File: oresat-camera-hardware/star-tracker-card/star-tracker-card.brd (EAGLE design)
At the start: 99.8 x 94.7 mm, 319 parts, among them J1 ORESAT-DEBUG-CONNECTOR-CARD, J100 DM3BT-DSF-PEJS, J101 3-1734592-64-1734592-0, J102 FTSH-105-XX-X-DV-K, J4 TFM-120-01-L-D-RA, Q1 MMBT2907, Q2 PMV45EN, Q3 DMP2240UDM, Q4 PMV45EN, Q5 MOSFET-PCH-SOT23-6, Q6 MOSFET-PCH-SOT23-6, U1 RCLAMP0504FB, U10 TLVH431, U11 TCAN330, U12 MIC842LYC5, U13 MIC842LYC5, U14 MAX4211FETE, U15 TPS62112, U16 MAX7310ATE, U2 TPS2051CDBVR, U4 SN74LVC1G07DCK, U5 SN74LVC8T245MPWREPPW24-M, U6 CLVCH16T245MDGGREP, U7 OSD3358-512M-BSM, U8 TLV70028QDDCRQ1, U9 TCA9509DGKRDGK8-M, Y1 24MHz, Y2 ABS07-32.768KHZ-T

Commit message: implemented design review changes. Cleaned up the repo a bit. Added generic SPI EEPROM footprint for booting
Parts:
- removed J2: (no value), SparkFun-Connectors:1X02_LONGPADS
- removed TP32, TP33, TP34: TEST-POINT3X4, SparkFun-Connectors:PAD.03X.04
- added C40: 0.1uF, oresat-rcl:.0603-A
- added JP1: JUMPER-SMT_2_NO_SILK, SparkFun-Jumpers:SMT-JUMPER_2_NO_SILK
- added TP67, TP68: TEST-POINT, Tova:2MM-TEST-POINT
- added TP69: TEST-POINT3X4, SparkFun-Connectors:PAD.03X.04
- added U17: 25AAXX, U-Generic-SPI-EEPROM:SOIC8
- R59, R60: value 47k -> DNP
- moved R59 65.2 mm to (81.5, 59.5), turned to 180 degrees
- moved R60 64.1 mm to (81.5, 57.5), turned to 0 degrees
- moved TP31 59.6 mm to (7.50, 57.5)
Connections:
- removed net 5V_IN: C14.1, J2.2, U7.P10, U7.R10, U7.T10
- new net N$110: R59.1, R60.2, U17.3
- new net N$111: TP69.P$1, U17.7
- new net N$112: J102.10, JP1.2
- net 3.3V: now also C40.2, R60.1, U17.8
- net 5V: now also C14.1, U7.P10, U7.R10, U7.T10; no longer J2.1
- net GND: now also C40.1, R59.2, U17.4
- net N$28: now also U17.6; no longer TP33.P$1
- net N$29: now also U17.2; no longer TP31.P$1
- net N$30: now also U17.5; no longer TP32.P$1
- net N$31: now also U17.1; no longer TP34.P$1
- net N$385: no longer R59.1, R60.1
- net N$657: now also TP31.P$1; no longer J102.10
- net PB6/SCL: now also TP67.1; no longer R60.2
- net PB7/SDA: now also TP68.1; no longer R59.2
- net RESET#: now also JP1.1
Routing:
- net N$112: track 0.00 -> 50.0 mm
- net 3.3V: track 93.6 -> 131.1 mm, vias 44 -> 46
- net N$29: track 4.57 -> 22.4 mm
- net N$30: track 4.87 -> 21.4 mm
- net N$31: track 4.19 -> 19.2 mm
- net N$28: track 4.06 -> 16.7 mm
- net N$385: track 15.7 -> 4.54 mm, vias 2 -> 1
- net N$111: track 0.00 -> 8.22 mm
- net N$110: track 0.00 -> 6.70 mm
- net 5V: track 11.8 -> 17.1 mm, vias 3 -> 18
- net RESET#: track 26.3 -> 31.3 mm, vias 2 -> 3
- net PB6/SCL: track 3.38 -> 6.86 mm, vias 0 -> 1
- net USB_HO_VBUS: track 15.6 -> 18.2 mm
- net N$657: track 55.4 -> 57.5 mm
- net PB7/SDA: track 6.96 -> 5.48 mm, vias 0 -> 1
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- added copper zone on layer 15, net 5V
- removed copper zone on layer 1, net 5V_IN
- removed copper zone on layer 15, net 5V_IN
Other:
- board text removed: "VBUS PWR"

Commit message: added part number attributes
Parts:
- C18: value 0.1uF, 6.3V -> 0.1uF
- C32, C35: value 1u -> 1uF
- R13: value 1M, 1% -> 1M
- R27: value 1M, DNI -> DNP
- R28: value 10.0K -> 10k

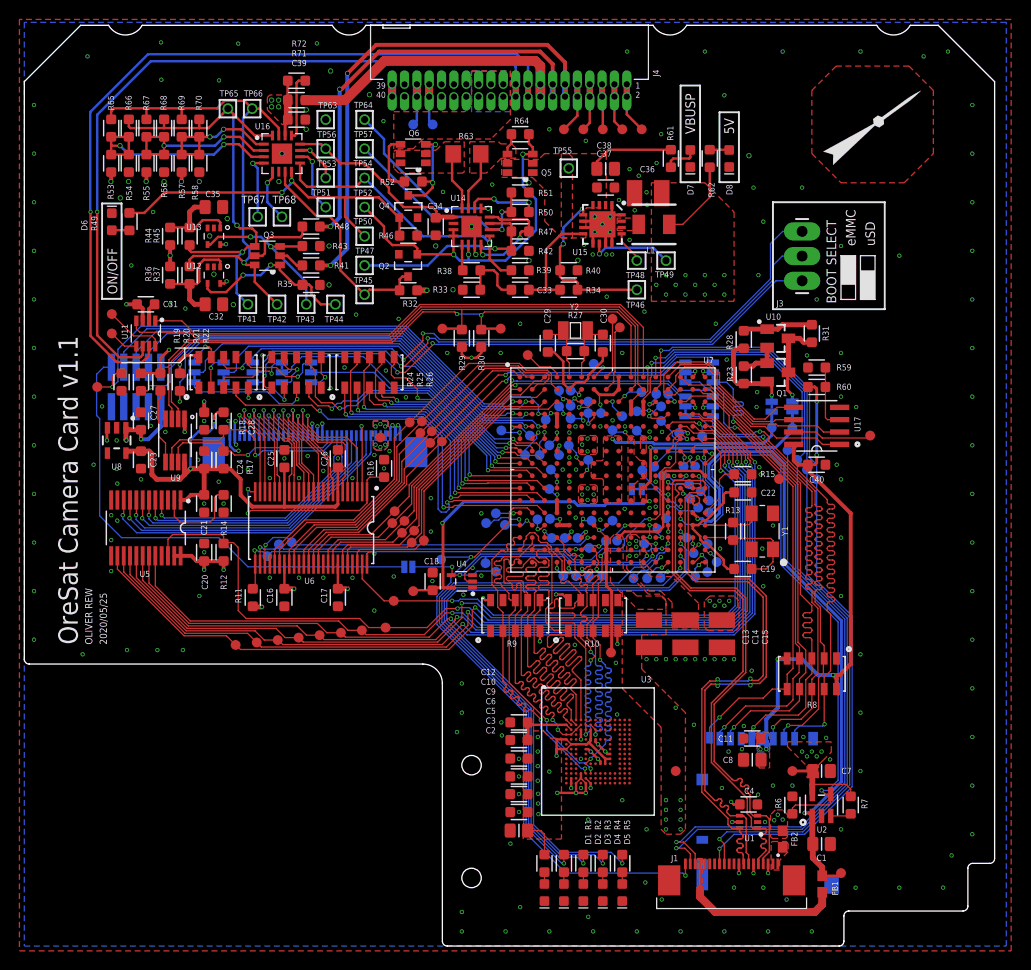
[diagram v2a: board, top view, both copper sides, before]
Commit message: updated board and BOM with rev1.1 notes
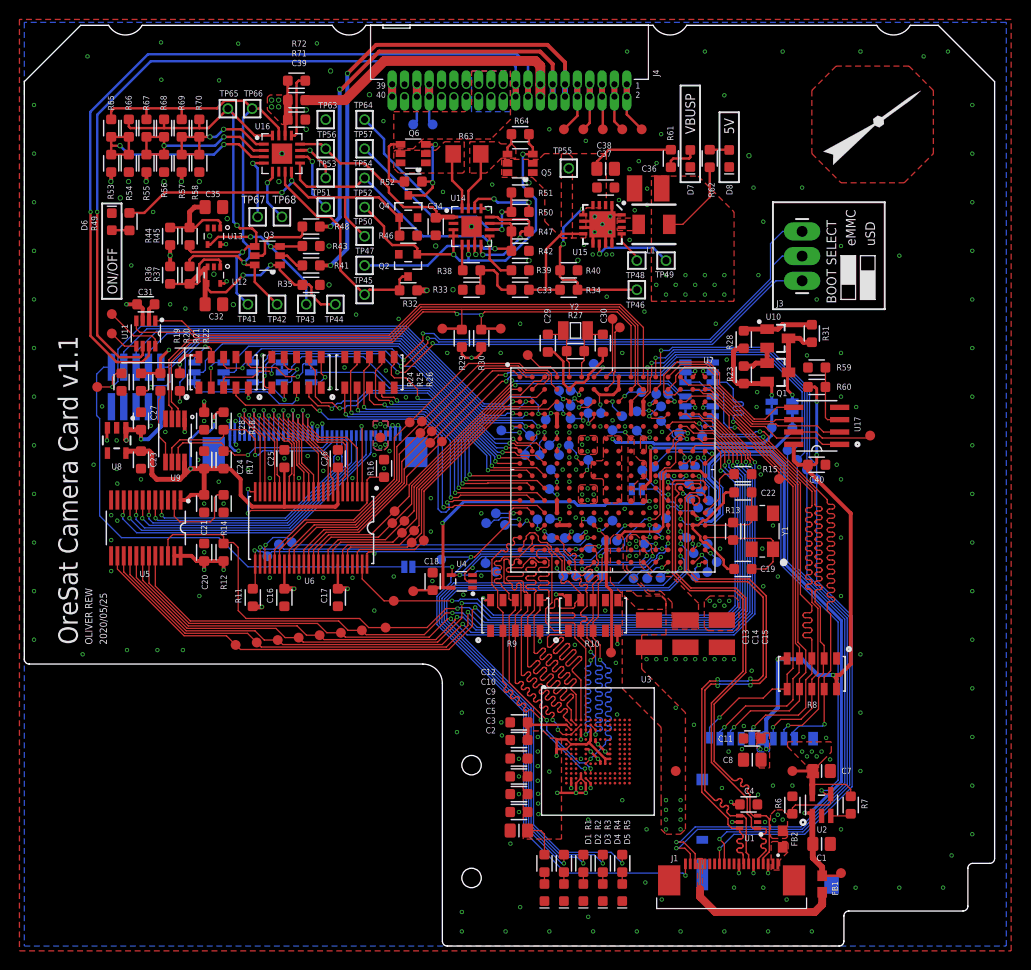
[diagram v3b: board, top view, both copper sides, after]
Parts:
- moved C36 0.50 mm to (64.2, 77.9)
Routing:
- net N$25: track 11.3 -> 13.8 mm
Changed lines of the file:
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@@
 <?xml version="1.0" encoding="utf-8"?>
 <!DOCTYPE eagle SYSTEM "eagle.dtd">
-<eagle version="9.6.1">
+<eagle version="9.6.2">
 <drawing>
 <settings>
@@
 <attribute name="VALUE" x="58.6" y="76.4125" size="0.8" layer="27" font="vector" ratio="15"/>
 </element>
-<element name="C36" library="oresat-rcl" package="C1210" value="22uF" x="64.1625" y="77.425" smashed="yes" rot="R180">
-<attribute name="NAME" x="64.85625" y="80.21875" size="0.635" layer="25" font="vector" ratio="20" rot="R180"/>
-<attribute name="NAME" x="64.1625" y="77.425" size="0.4" layer="33" ratio="15" rot="R180" align="center"/>
-<attribute name="VALUE" x="65.6625" y="79.225" size="0.8" layer="27" font="vector" ratio="15" rot="R180"/>
+<element name="C36" library="oresat-rcl" package="C1210" value="22uF" x="64.1625" y="77.925" smashed="yes" rot="R180">
+<attribute name="NAME" x="65.04375" y="80.28125" size="0.635" layer="25" font="vector" ratio="20" rot="R180"/>
+<attribute name="NAME" x="64.1625" y="77.925" size="0.4" layer="33" ratio="15" rot="R180" align="center"/>
+<attribute name="VALUE" x="65.6625" y="79.725" size="0.8" layer="27" font="vector" ratio="15" rot="R180"/>
 </element>
 <element name="TP49" library="Tova" package="2MM-TEST-POINT" value="TEST-POINT" x="66" y="70.5" smashed="yes" rot="R270">
@@
 </element>
 <element name="R15" library="oresat-rcl" package=".0603-A" value="10k" x="73.90625" y="48.53125" smashed="yes" rot="R180">
-<attribute name="NAME" x="75.69375" y="48.23125" size="0.635" layer="25" font="vector" ratio="20"/>
+<attribute name="NAME" x="75.94375" y="48.73125" size="0.635" layer="25" font="vector" ratio="20"/>
 <attribute name="NAME" x="73.90625" y="48.53125" size="0.3" layer="33" ratio="15" rot="R180" align="center"/>
 <attribute name="VALUE" x="75.30625" y="50.28125" size="0.8" layer="27" font="vector" ratio="15" rot="R180"/>
@@
 <attribute name="DPN" value="THGBMJG7C2LBAU8-ND" x="59" y="20" size="1.778" layer="27" display="off"/>
 <attribute name="MPN" value="THGBMJG7C2LBAU8" x="59" y="20" size="1.778" layer="27" display="off"/>
-<attribute name="NAME" x="63.425" y="27.1125" size="0.635" layer="25" font="vector" ratio="20"/>
 <attribute name="NAME" x="59" y="20" size="1.5" layer="33" ratio="15" align="center"/>
+<attribute name="NAME" x="63.425" y="27.1125" size="0.635" layer="25" font="vector" ratio="20"/>
 <attribute name="VALUE" x="53.4" y="12.4" size="0.8" layer="27" font="vector" ratio="15"/>
 </element>
@@
 <element name="C31" library="oresat-rcl" package=".0603-A" value="0.1uF" x="12.5" y="66" smashed="yes" rot="R180">
 <attribute name="NAME" x="12.5" y="66" size="0.2" layer="33" ratio="15" rot="R180" align="center"/>
-<attribute name="NAME" x="14.2625" y="65.70625" size="0.635" layer="25" font="vector" ratio="20"/>
+<attribute name="NAME" x="11.7" y="66.95625" size="0.635" layer="25" font="vector" ratio="20"/>
 <attribute name="VALUE" x="13.3" y="67.35" size="0.8" layer="27" font="vector" ratio="15" rot="R180"/>
 </element>
@@
 </element>
 <element name="R18" library="oresat-rcl" package=".0603-A" value="4.7k" x="20.5" y="54" smashed="yes" rot="R270">
-<attribute name="NAME" x="22.75" y="52.5625" size="0.635" layer="25" font="vector" ratio="20" rot="R90"/>
+<attribute name="NAME" x="23.75" y="52.5625" size="0.635" layer="25" font="vector" ratio="20" rot="R90"/>
 <attribute name="NAME" x="20.5" y="54" size="0.3" layer="33" ratio="15" rot="R270" align="center"/>
 <attribute name="VALUE" x="18.75" y="55.4" size="0.8" layer="27" font="vector" ratio="15" rot="R270"/>
@@
 </element>
 <element name="C28" library="oresat-rcl" package=".0603-A" value="0.1uF" x="18.5" y="54" smashed="yes" rot="R270">
-<attribute name="NAME" x="23.6875" y="52.5625" size="0.635" layer="25" font="vector" ratio="20" rot="R90"/>
+<attribute name="NAME" x="22.6875" y="52.5625" size="0.635" layer="25" font="vector" ratio="20" rot="R90"/>
 <attribute name="NAME" x="18.5" y="54" size="0.3" layer="33" ratio="15" rot="R270" align="center"/>
 <attribute name="VALUE" x="16.75" y="55.4" size="0.8" layer="27" font="vector" ratio="15" rot="R270"/>
@@
 <attribute name="DPN" value="576-2927-1-ND" x="19.5" y="73" size="1.778" layer="27" rot="R180" display="off"/>
 <attribute name="MPN" value="MIC842LYC5" x="19.5" y="73" size="1.778" layer="27" rot="R180" display="off"/>
-<attribute name="NAME" x="18.23" y="74.27" size="0.635" layer="25" font="vector" ratio="20" rot="R180"/>
+<attribute name="NAME" x="22.48" y="73.3325" size="0.635" layer="25" font="vector" ratio="20" rot="R180"/>
 </element>
 <element name="U12" library="U-Microchip-MIC842-Comparator" package="SC70-5" value="MIC842LYC5" x="19.5" y="69" smashed="yes" rot="R180">
 <attribute name="DPN" value="576-2927-1-ND" x="19.5" y="69" size="1.778" layer="27" rot="R180" display="off"/>
 <attribute name="MPN" value="MIC842LYC5" x="19.5" y="69" size="1.778" layer="27" rot="R180" display="off"/>
-<attribute name="NAME" x="18.23" y="70.27" size="0.635" layer="25" font="vector" ratio="20" rot="R180"/>
+<attribute name="NAME" x="22.9175" y="68.645" size="0.635" layer="25" font="vector" ratio="20" rot="R180"/>
 </element>
 <element name="TP67" library="Tova" package="2MM-TEST-POINT" value="TEST-POINT" x="24" y="75" smashed="yes">
@@
 <wire x1="59.78125" y1="71.8125" x2="64.6875" y2="71.8125" width="0.254" layer="16"/>
 <polygon width="0.127" layer="1" isolate="0.2" thermals="no">
-<vertex x="64.5" y="78.5"/>
-<vertex x="70" y="78.5"/>
+<vertex x="64.5" y="79.1875"/>
+<vertex x="69.3125" y="79.1875"/>
 <vertex x="73" y="75.5"/>
 <vertex x="73" y="66.3125"/>
@@
 <wire x1="82.3125" y1="22.8125" x2="82.125" y2="22.625" width="0.127" layer="16"/>
 <wire x1="82.125" y1="22.625" x2="79.6875" y2="22.625" width="0.127" layer="16"/>
-<wire x1="79.6875" y1="22.625" x2="79.23125" y2="22.16875" width="0.127" layer="16"/>
-<wire x1="79.23125" y1="21.325" x2="79.23125" y2="22.16875" width="0.127" layer="16"/>
+<wire x1="79.6875" y1="22.625" x2="78.809375" y2="21.746875" width="0.127" layer="16"/>
+<wire x1="79.23125" y1="21.325" x2="78.809375" y2="21.746875" width="0.127" layer="16"/>
 <via x="82.3125" y="22.8125" extent="1-16" drill="0.254"/>
 <wire x1="82.27" y1="26.4252" x2="82.27" y2="22.855" width="0.127" layer="1"/>
@@
 <wire x1="20.15625" y1="70.4375" x2="20.15625" y2="70" width="0.254" layer="1"/>
 <wire x1="18" y1="68.34375" x2="18" y2="70.119" width="0.254" layer="1"/>
-<wire x1="18.6" y1="66" x2="17.5" y2="66" width="0.508" layer="1"/>
-<wire x1="17.5" y1="66" x2="17" y2="66.5" width="0.508" layer="1"/>
-<wire x1="17" y1="66.5" x2="17" y2="68.1" width="0.508" layer="1"/>
+<wire x1="18.6" y1="66" x2="18.6" y2="69.7" width="0.508" layer="1"/>
+<wire x1="17" y1="68.1" x2="18.6" y2="69.7" width="0.508" layer="1"/>
 <contactref element="U12" pad="1"/>
 <wire x1="20.15" y1="69.85" x2="20.15" y2="69.99375" width="0.254" layer="1"/>
@@
 <via x="61.1625" y="76.725" extent="1-16" drill="0.254"/>
 <via x="62.78125" y="75.675" extent="1-16" drill="0.254"/>
-<via x="64" y="77.525" extent="1-16" drill="0.254"/>
-<via x="63.2" y="79.225" extent="1-16" drill="0.254"/>
+<via x="64.0625" y="77.9" extent="1-16" drill="0.254"/>
+<via x="63.2" y="80.725" extent="1-16" drill="0.254"/>
 <via x="62.2625" y="72.625" extent="1-16" drill="0.254"/>
 <via x="64.0625" y="76.225" extent="1-16" drill="0.254"/>

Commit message: minor DRC fixup
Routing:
- net N$25: track 13.8 -> 11.1 mm
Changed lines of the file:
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@@
 <contactref element="C32" pad="1"/>
 <wire x1="15" y1="68.1" x2="17" y2="68.1" width="0.254" layer="1"/>
-<wire x1="17" y1="68.1" x2="17.75625" y2="68.1" width="0.254" layer="1"/>
+<wire x1="17" y1="68.1" x2="17.0625" y2="68.1" width="0.254" layer="1"/>
+<wire x1="17.0625" y1="68.1" x2="17.75625" y2="68.1" width="0.254" layer="1"/>
 <wire x1="17.75625" y1="68.1" x2="18" y2="68.34375" width="0.254" layer="1"/>
 <wire x1="18" y1="70.119" x2="18.46875" y2="70.58775" width="0.254" layer="1"/>
@@
 <wire x1="20.15625" y1="70.4375" x2="20.15625" y2="70" width="0.254" layer="1"/>
 <wire x1="18" y1="68.34375" x2="18" y2="70.119" width="0.254" layer="1"/>
-<wire x1="18.6" y1="66" x2="18.6" y2="69.7" width="0.508" layer="1"/>
-<wire x1="17" y1="68.1" x2="18.6" y2="69.7" width="0.508" layer="1"/>
 <contactref element="U12" pad="1"/>
 <wire x1="20.15" y1="69.85" x2="20.15" y2="69.99375" width="0.254" layer="1"/>
 <wire x1="20.15" y1="69.99375" x2="20.15625" y2="70" width="0.254" layer="1"/>
+<wire x1="18.6" y1="66" x2="17.75" y2="66" width="0.508" layer="1"/>
+<wire x1="17.0625" y1="66.6875" x2="17.0625" y2="68.1" width="0.508" layer="1"/>
+<wire x1="17.75" y1="66" x2="17.0625" y2="66.6875" width="0.508" layer="1"/>
 </signal>
 <signal name="OSC1_IN1">

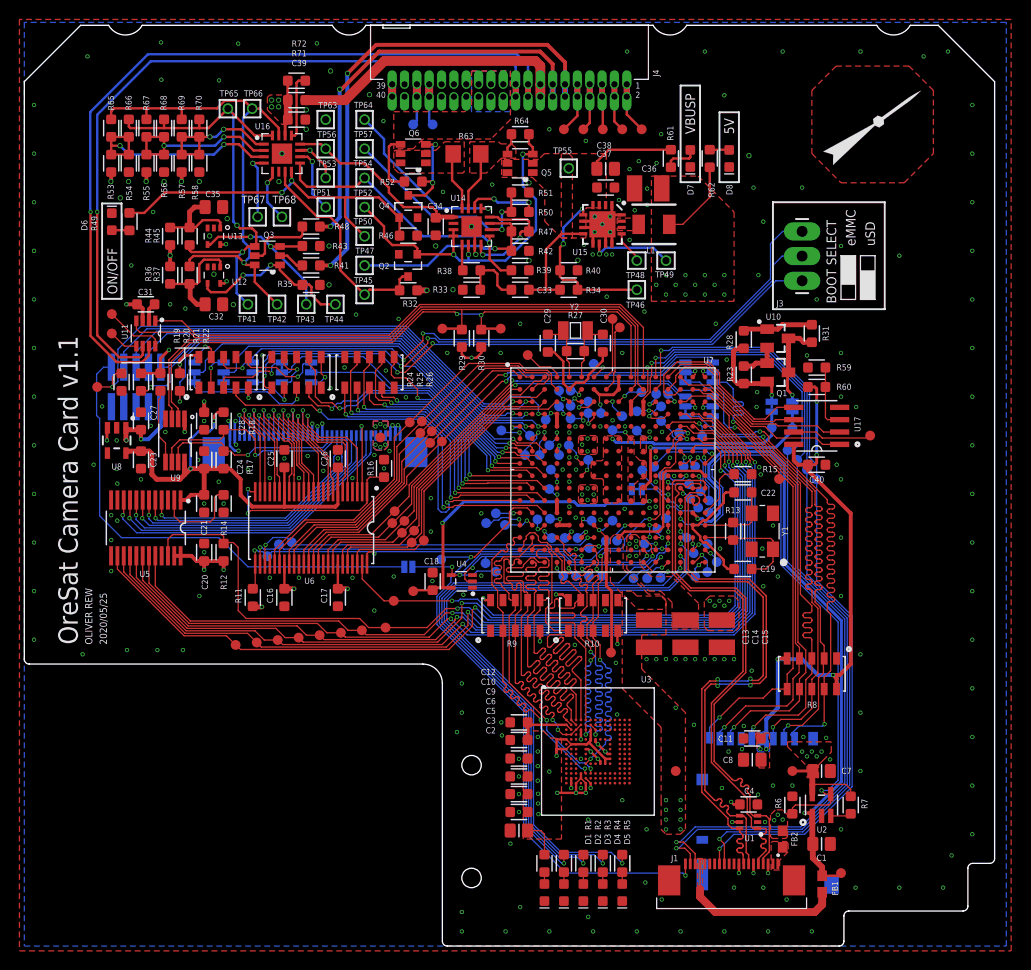
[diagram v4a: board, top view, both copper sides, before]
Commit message: added new outline DXF and updated board
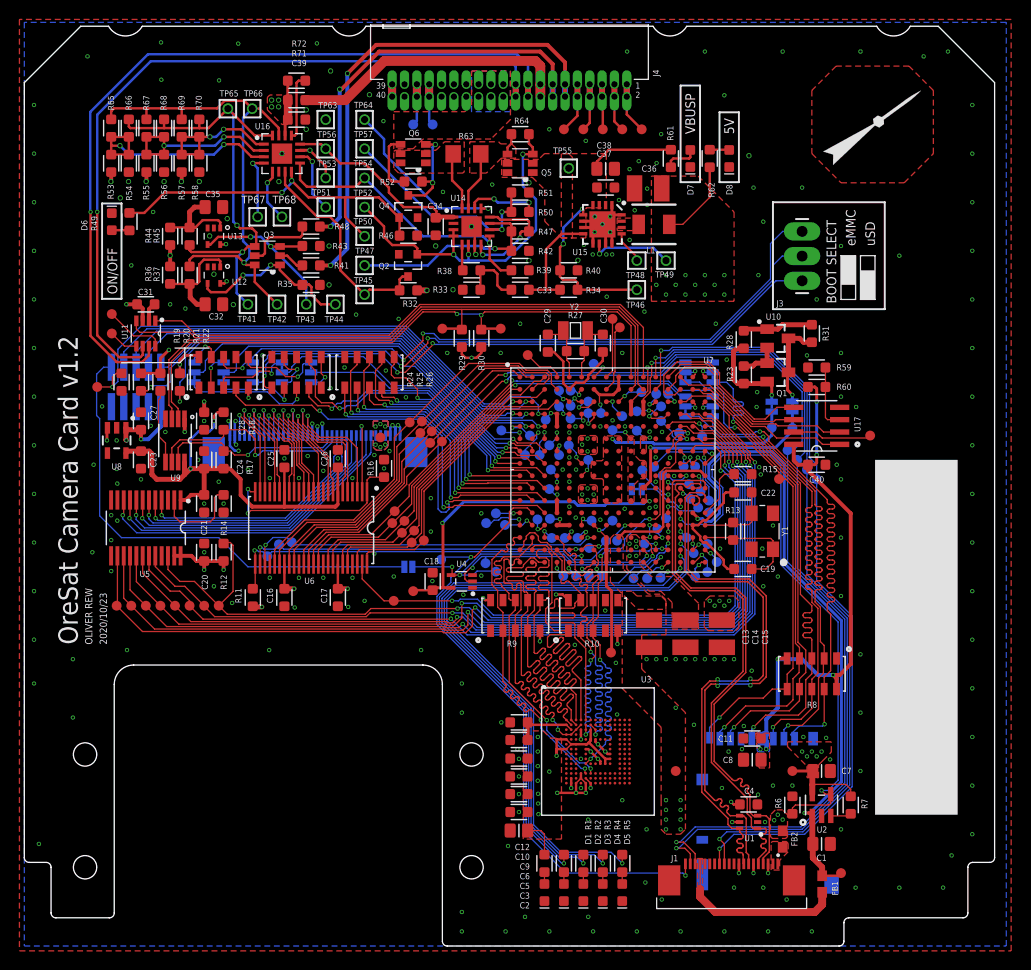
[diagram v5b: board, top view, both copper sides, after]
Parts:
- U$1: device oresat-cards:ORESAT-CAMERA-CARD-V0.1-3XRF -> oresat-cards:ORESAT-CAMERA-CARD-V2
- moved TP12 17.3 mm to (20.0, 35.0)
- moved TP11 16.4 mm to (18.5, 35.0)
- moved TP10 15.8 mm to (17.0, 35.0)
- moved TP9 15.2 mm to (15.5, 35.0)
- moved TP8 14.6 mm to (14.0, 35.0)
- moved TP7 14.0 mm to (12.5, 35.0)
- moved TP6 13.4 mm to (11.0, 35.0)
- moved TP5 12.9 mm to (9.50, 35.0)
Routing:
- net CLK_EN: track 89.6 -> 86.9 mm
- net RESET: track 92.9 -> 90.8 mm
- net STANDBY: track 94.6 -> 92.8 mm
- net CAM_OE: track 90.8 -> 89.6 mm
- net VREG_EN: track 92.1 -> 93.0 mm
- net INPUT_EN: track 94.3 -> 94.9 mm
- net SADDR: track 94.9 -> 94.4 mm
- net GND: vias 285 -> 291
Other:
- board size 99.8 x 94.7 mm -> 99.8 x 94.6 mm
- board text added: "2020/10/23"
- board text added: "OreSat Camera Card v1.2"
- board text removed: "2020/05/25"
- board text removed: "OreSat Camera Card v1.1"
